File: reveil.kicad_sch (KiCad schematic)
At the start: 8 parts, among them SW2 SW_Push

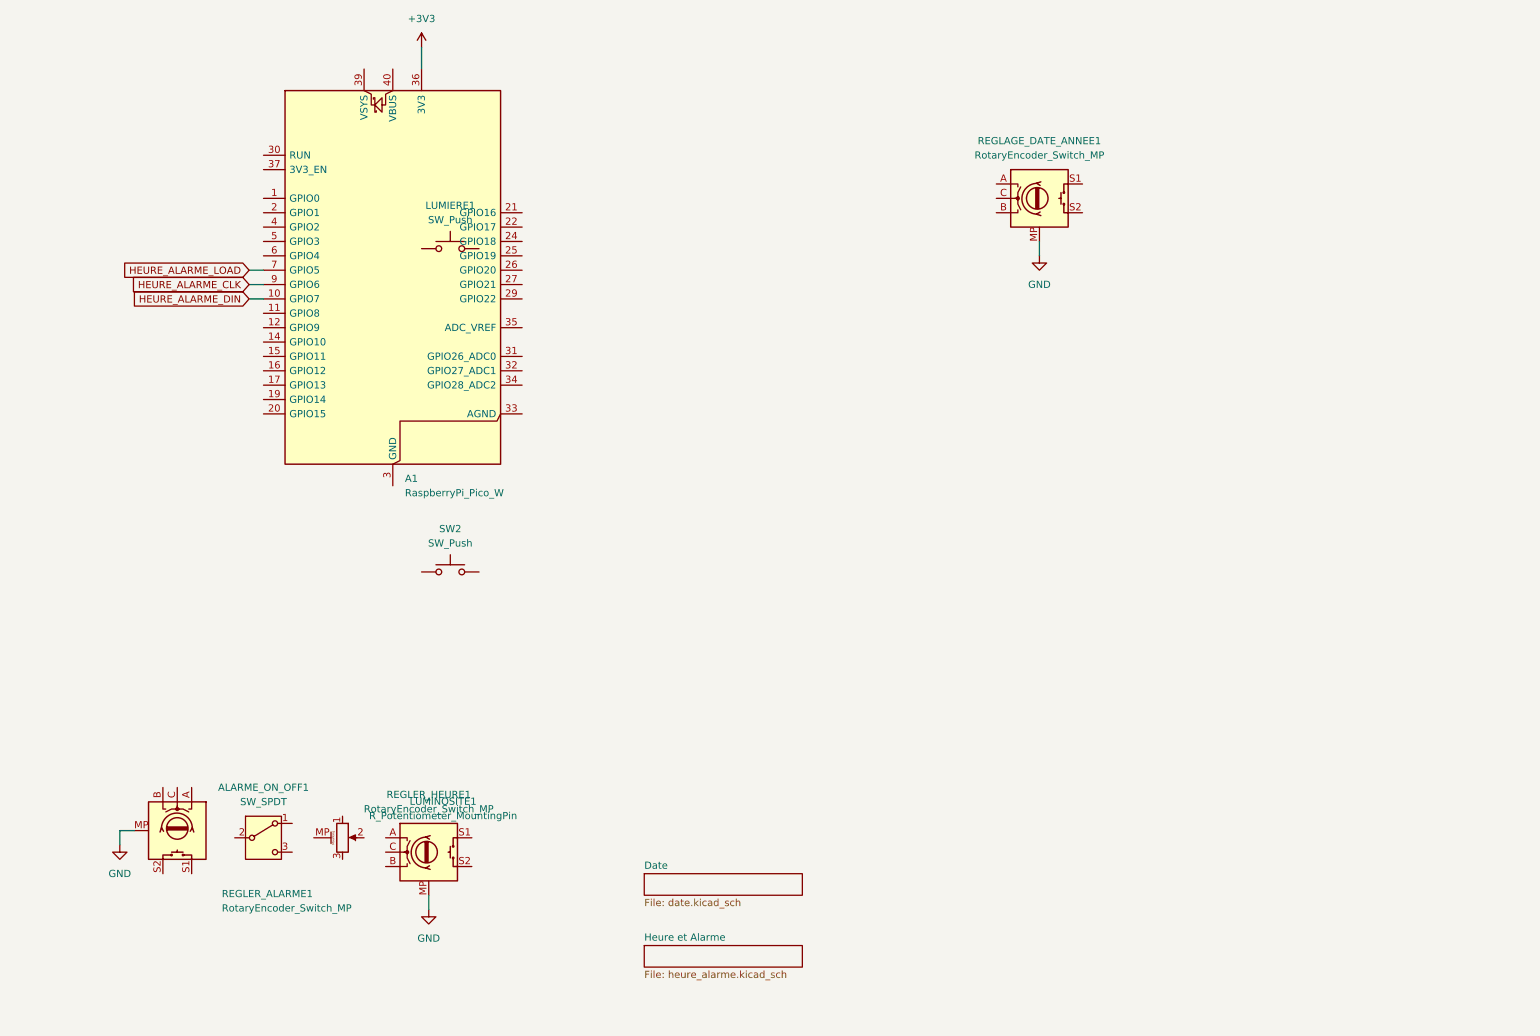
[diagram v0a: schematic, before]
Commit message: Added VBUS and misc
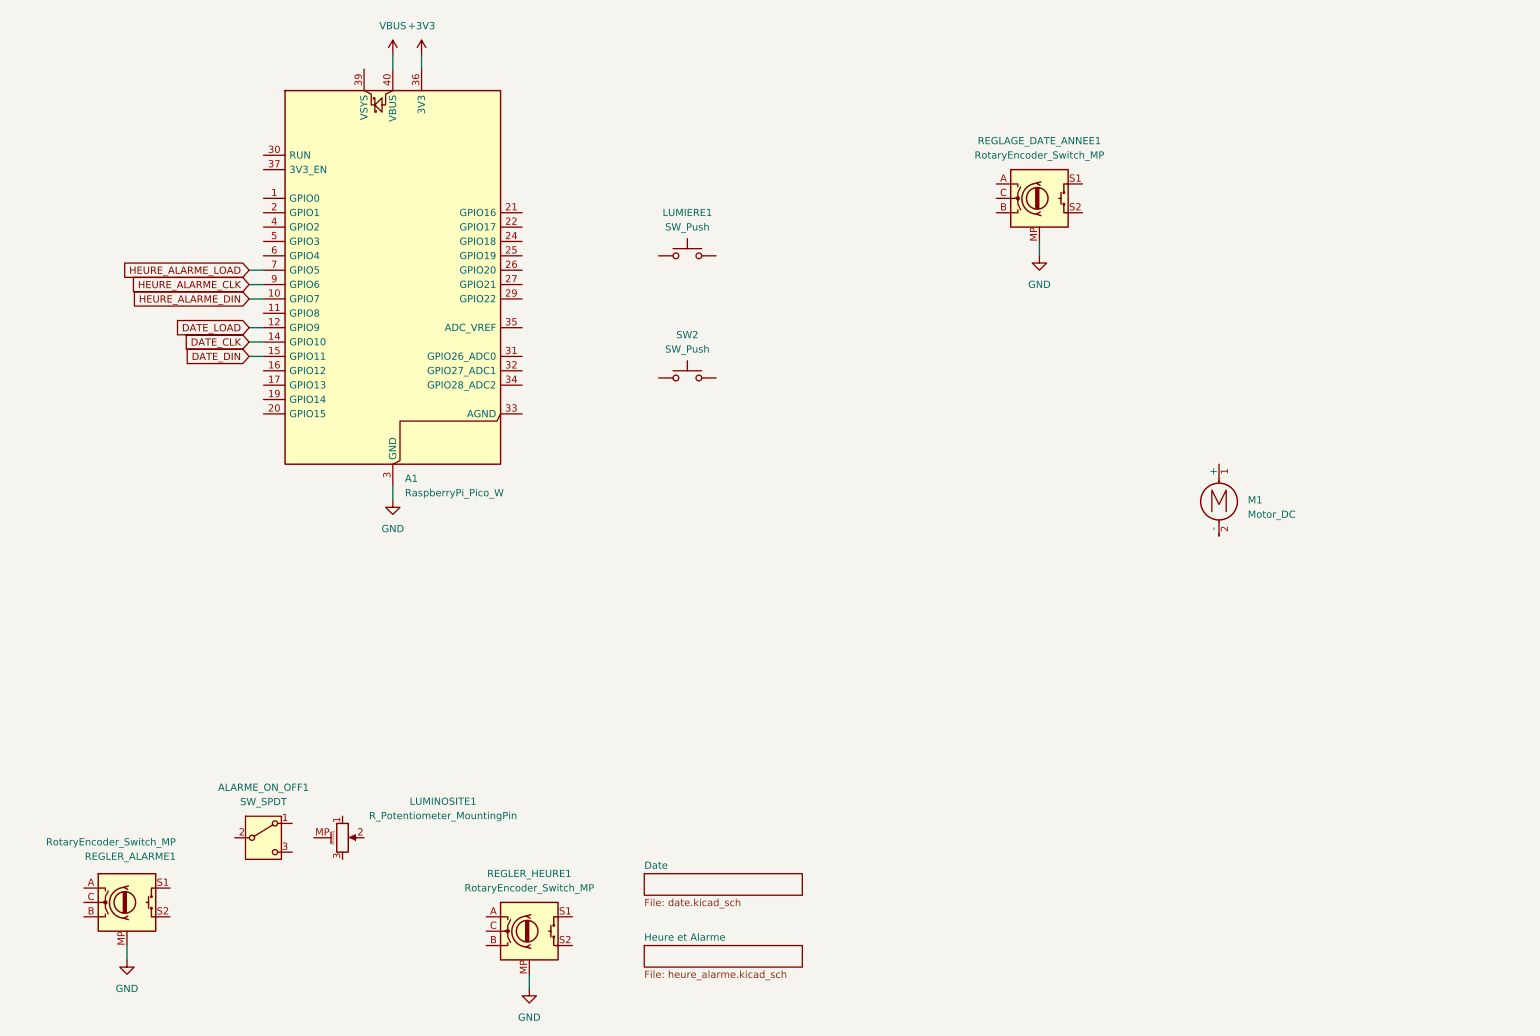
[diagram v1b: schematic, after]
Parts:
- added M1: Motor_DC, symbol Motor:Motor_DC
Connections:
- net GND: now also A1.13 (GND), A1.18 (GND), A1.23 (GND), A1.28 (GND), A1.3 (GND), A1.38 (GND), A1.8 (GND)
- net DATE_LOAD: now reaches A1.12 (GPIO9)
- net DATE_CLK: now reaches A1.14 (GPIO10)
- net DATE_DIN: now reaches A1.15 (GPIO11)
- net VBUS: now reaches A1.40 (VBUS)
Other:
- moved on the sheet: LUMIERE1, REGLER_ALARME1, REGLER_HEURE1, SW2

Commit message: un peu plus de composants connectés
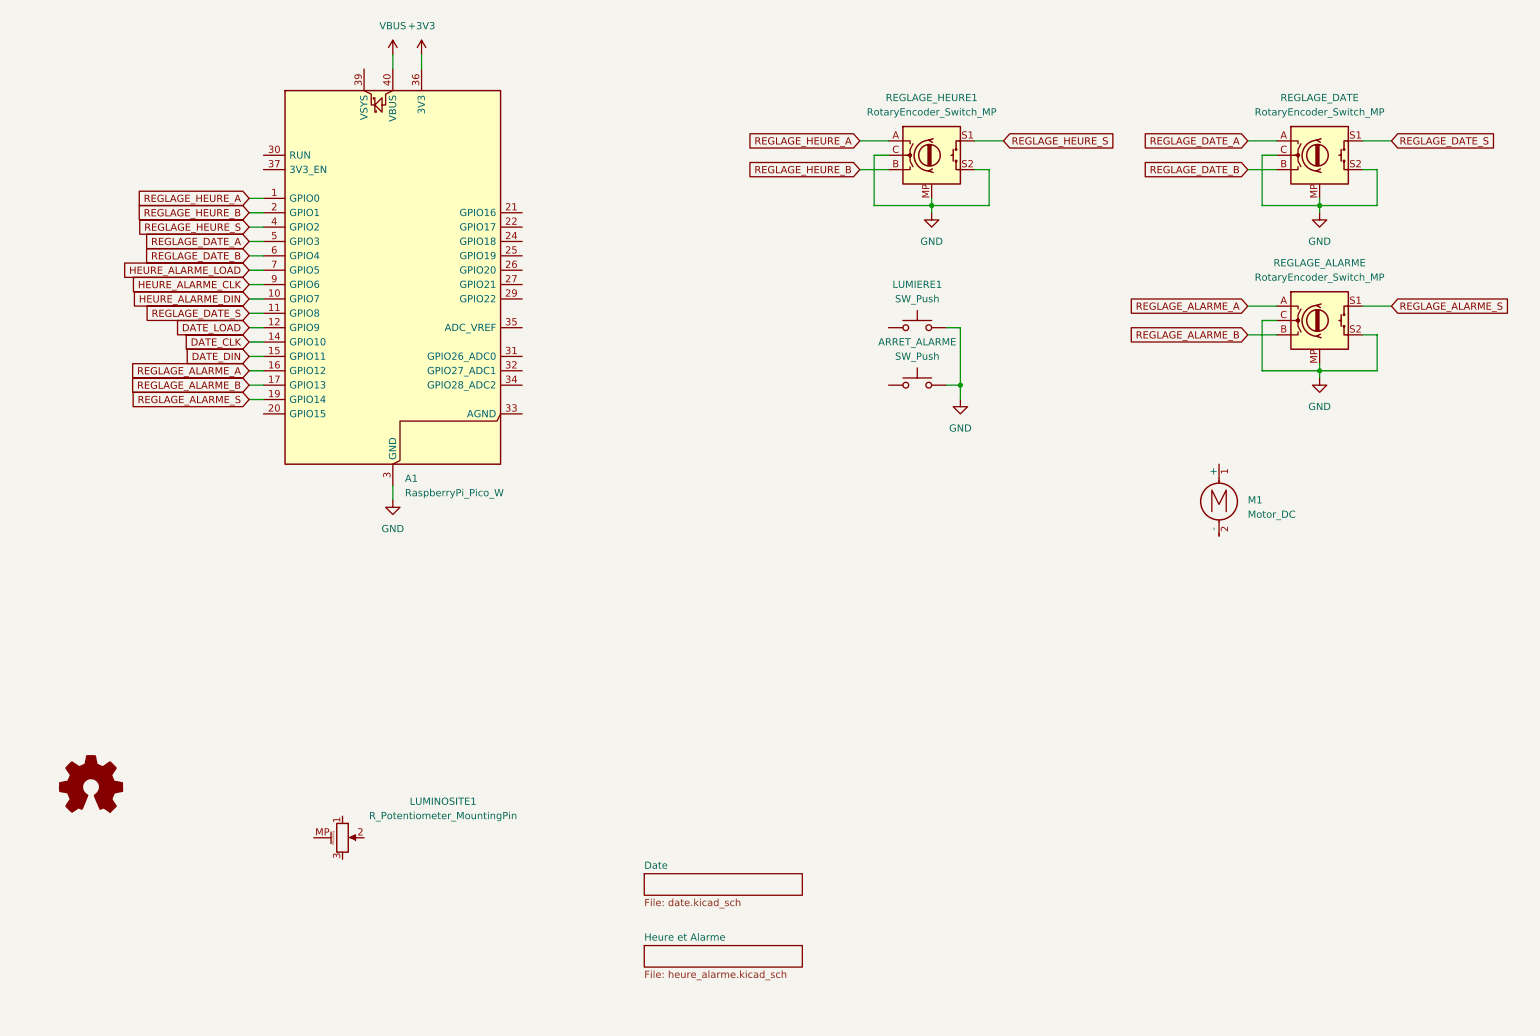
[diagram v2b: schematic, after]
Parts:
- removed ALARME_ON_OFF1: SW_SPDT, symbol Switch:SW_SPDT
- removed REGLAGE_DATE_ANNEE1, REGLER_ALARME1: RotaryEncoder_Switch_MP, Rotary_Encoder:RotaryEncoder_Alps_EC11E-Switch_Vertical_H20mm_MountingHoles, symbol Device:RotaryEncoder_Switch_MP
- added REGLAGE_ALARME, REGLAGE_DATE: RotaryEncoder_Switch_MP, Rotary_Encoder:RotaryEncoder_Alps_EC11E-Switch_Vertical_H20mm_MountingHoles, symbol Device:RotaryEncoder_Switch_MP
- renumbered SW2 to ARRET_ALARME, REGLER_HEURE1 to REGLAGE_HEURE1
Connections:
- net GND: now also ARRET_ALARME.2, LUMIERE1.2, REGLAGE_HEURE1.C, REGLAGE_HEURE1.S2, REGLAGE_ALARME.C, REGLAGE_ALARME.MP, REGLAGE_ALARME.S2, REGLAGE_DATE.C, REGLAGE_DATE.MP, REGLAGE_DATE.S2
- net REGLAGE_HEURE_A: now reaches REGLAGE_HEURE1.A
- net REGLAGE_HEURE_A: now also A1.1 (GPIO0)
- net REGLAGE_HEURE_B: now reaches REGLAGE_HEURE1.B
- net REGLAGE_HEURE_B: now also A1.2 (GPIO1)
- net REGLAGE_HEURE_S: now reaches REGLAGE_HEURE1.S1
- net REGLAGE_HEURE_S: now also A1.4 (GPIO2)
- net REGLAGE_DATE_S: now reaches A1.11 (GPIO8)
- net REGLAGE_DATE_S: now also REGLAGE_DATE.S1
- net REGLAGE_ALARME_A: now reaches A1.16 (GPIO12)
- net REGLAGE_ALARME_A: now also REGLAGE_ALARME.A
- net REGLAGE_ALARME_B: now reaches A1.17 (GPIO13)
- net REGLAGE_ALARME_B: now also REGLAGE_ALARME.B
- net REGLAGE_ALARME_S: now reaches A1.19 (GPIO14)
- net REGLAGE_ALARME_S: now also REGLAGE_ALARME.S1
- net REGLAGE_DATE_A: now reaches A1.5 (GPIO3)
- net REGLAGE_DATE_A: now also REGLAGE_DATE.A
- net REGLAGE_DATE_B: now reaches A1.6 (GPIO4)
- net REGLAGE_DATE_B: now also REGLAGE_DATE.B
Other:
- moved on the sheet: ARRET_ALARME, LUMIERE1, REGLAGE_HEURE1

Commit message: tous les composants sont ajoutés et connecté dans le schema
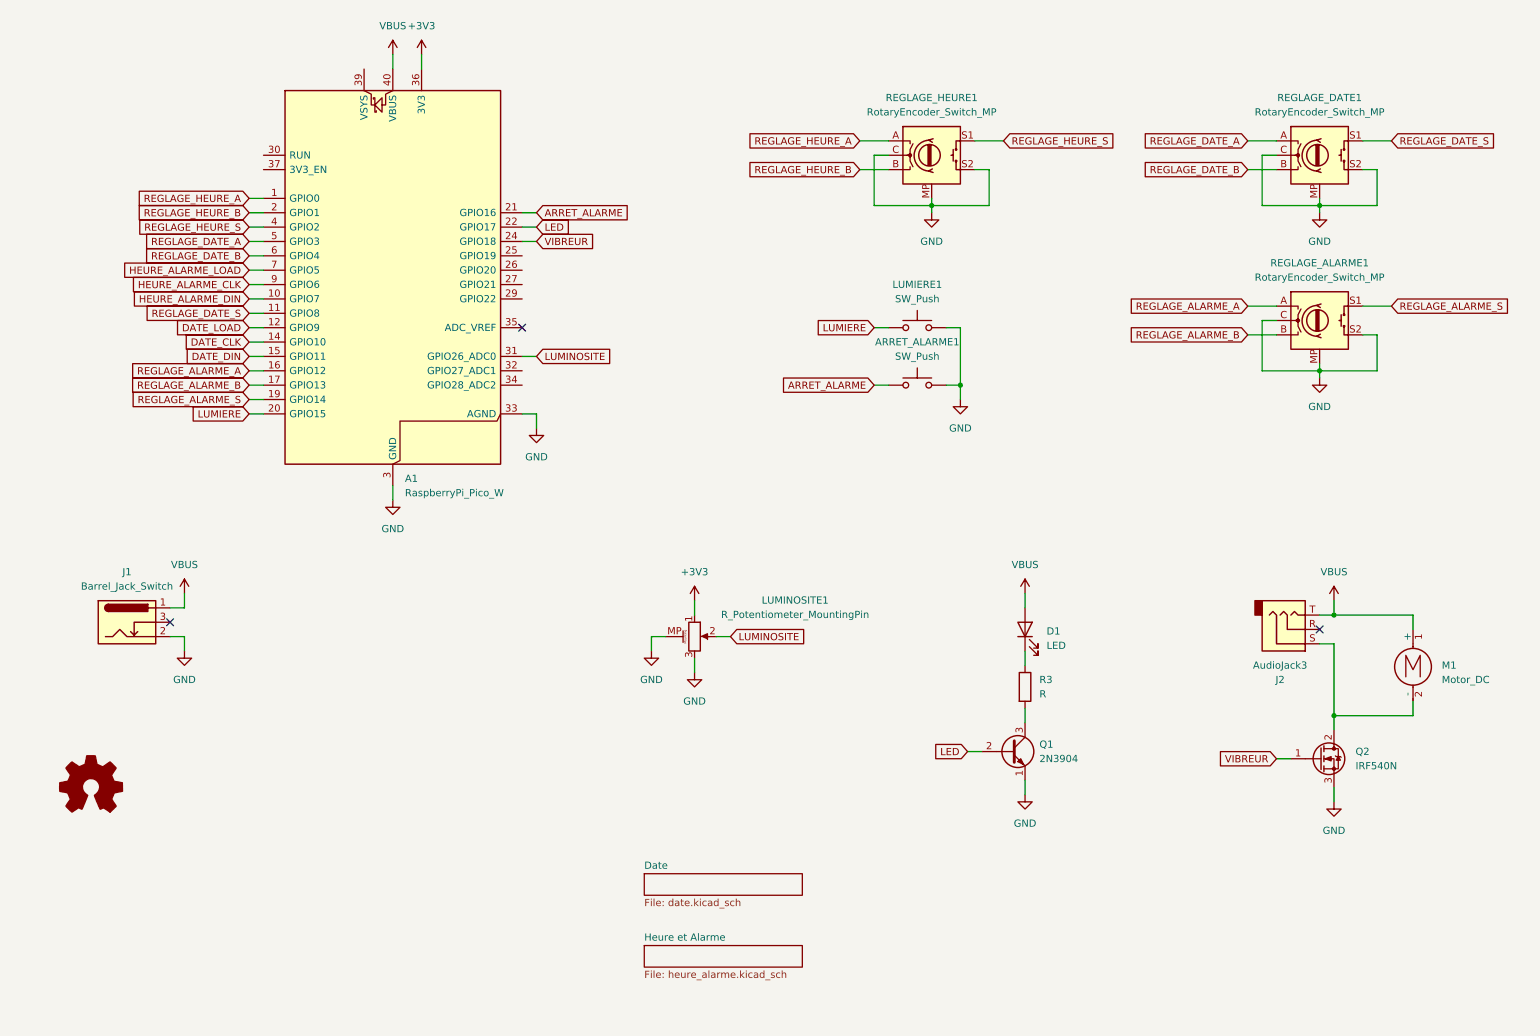
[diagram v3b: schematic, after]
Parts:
- added D1: LED, LED_THT:LED_D3.0mm, symbol Device:LED
- added J1: Barrel_Jack_Switch, symbol Connector:Barrel_Jack_Switch
- added J2: AudioJack3, symbol Connector_Audio:AudioJack3
- added Q1: 2N3904, Package_TO_SOT_THT:TO-92_HandSolder, symbol Transistor_BJT:2N3904
- added Q2: IRF540N, Package_TO_SOT_THT:TO-220-3_Horizontal_TabDown, symbol Transistor_FET:IRF540N
- added R3: R, Resistor_THT:R_Axial_DIN0207_L6.3mm_D2.5mm_P7.62mm_Horizontal, symbol Device:R
- renumbered ARRET_ALARME to ARRET_ALARME1, REGLAGE_ALARME to REGLAGE_ALARME1, REGLAGE_DATE to REGLAGE_DATE1
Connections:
- net +3V3: now also LUMINOSITE1.1
- net GND: now also A1.33 (AGND), LUMINOSITE1.3, LUMINOSITE1.MP (MountPin), J1.2, Q1.1 (E), Q2.3 (S)
- net VBUS: now also M1.1 (+), D1.2 (A), J1.1, J2.T
- net ARRET_ALARME: now reaches ARRET_ALARME1.1
- net ARRET_ALARME: now also A1.21 (GPIO16)
- net LUMIERE: now reaches LUMIERE1.1
- net LUMIERE: now also A1.20 (GPIO15)
- net LED: now reaches A1.22 (GPIO17)
- net LED: now also Q1.2 (B)
- net VIBREUR: now reaches A1.24 (GPIO18)
- net VIBREUR: now also Q2.1 (G)
- net LUMINOSITE: now reaches A1.31 (GPIO26_ADC0)
- net LUMINOSITE: now also LUMINOSITE1.2
- net at M1.2 (-): now also J2.S, Q2.2 (D)
- new net: D1.1 (K), R3.1
- new net: Q1.3 (C), R3.2
- no-connect marks 0 -> 3
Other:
- moved on the sheet: LUMINOSITE1, M1

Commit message: minor
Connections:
- no-connect marks 3 -> 12
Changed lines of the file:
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@@
+	)
+	(no_connect
+		(at 105.41 55.88)
+	)
+	(no_connect
+		(at 105.41 63.5)
+	)
+	(no_connect
+		(at 77.47 22.86)
+	)
+	(no_connect
+		(at 105.41 78.74)
+	)
+	(no_connect
+		(at 105.41 76.2)
+	)
+	(no_connect
+		(at 105.41 58.42)
 	)
 	(no_connect
@@
 	)
 	(no_connect
+		(at 105.41 60.96)
+	)
+	(no_connect
 		(at 43.18 120.65)
 	)
+	(no_connect
+		(at 59.69 38.1)
+	)
+	(no_connect
+		(at 59.69 40.64)
+	)
 	(wire

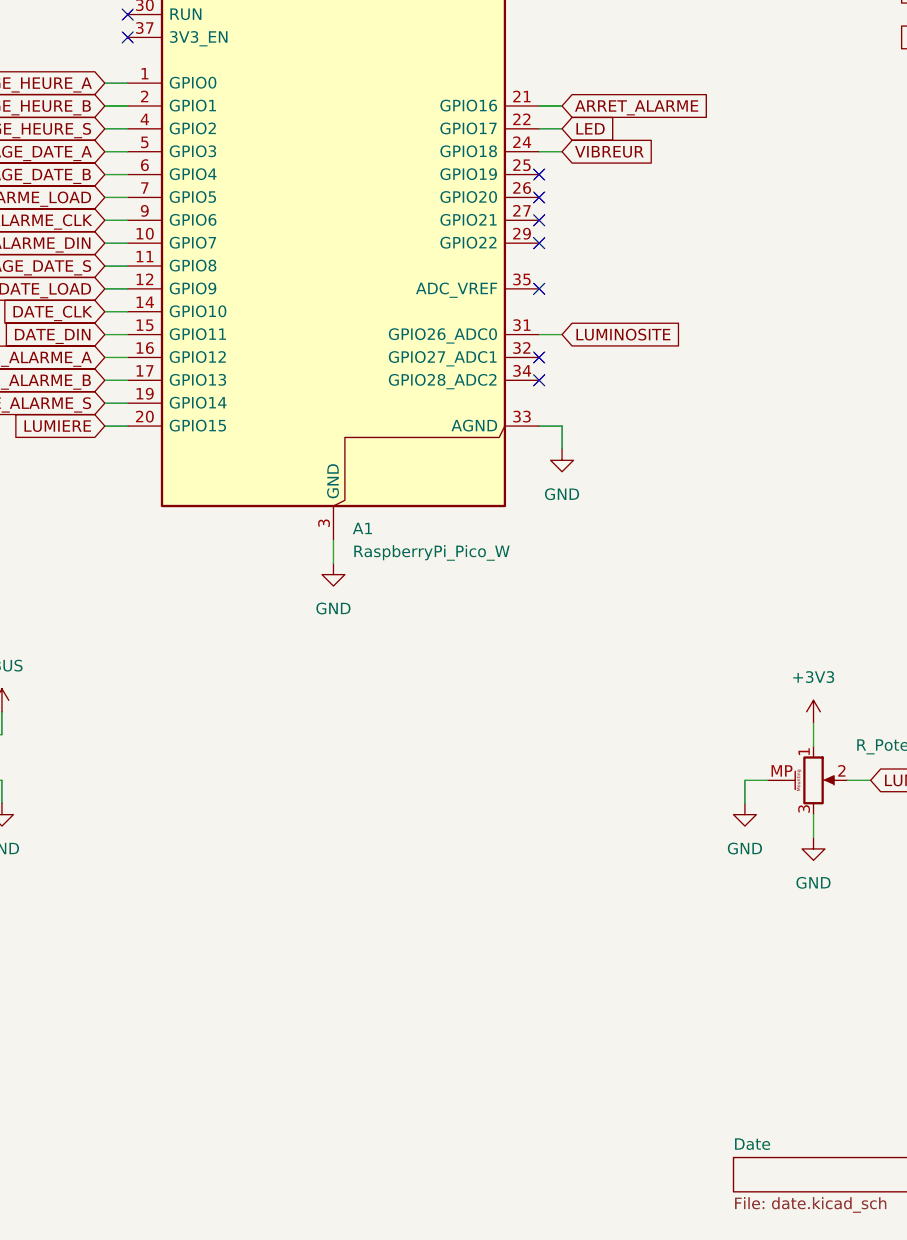
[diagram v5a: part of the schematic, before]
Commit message: ajout d'un switch pour activer l'alarme
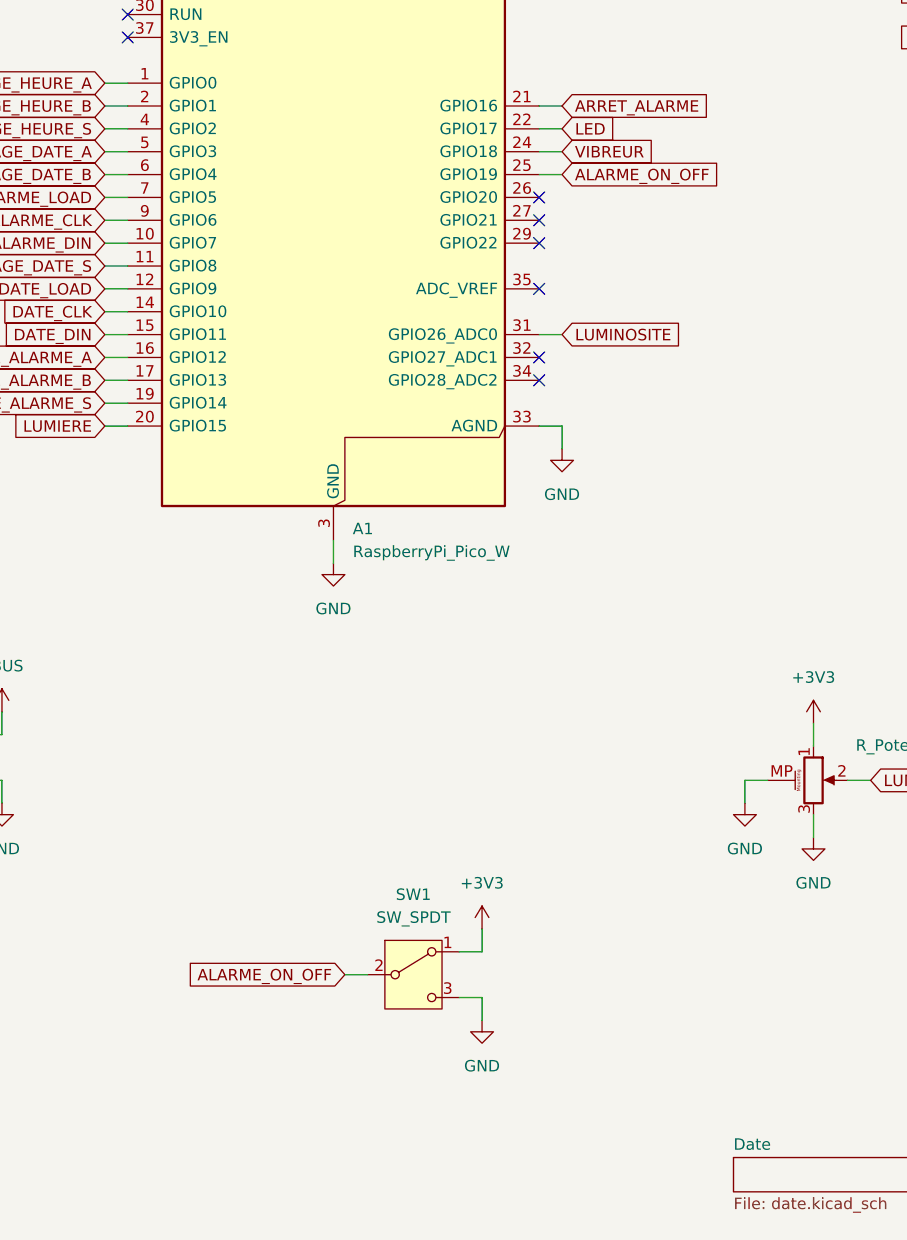
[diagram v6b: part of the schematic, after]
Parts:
- added SW1: SW_SPDT, Button_Switch_THT:SW_Slide-03_Wuerth-WS-SLTV_10x2.5x6.4_P2.54mm, symbol Switch:SW_SPDT
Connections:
- net +3V3: now also SW1.1 (A)
- net GND: now also SW1.3 (C)
- net ALARME_ON_OFF: now reaches A1.25 (GPIO19)
- net ALARME_ON_OFF: now also SW1.2 (B)
- no-connect marks 12 -> 11
